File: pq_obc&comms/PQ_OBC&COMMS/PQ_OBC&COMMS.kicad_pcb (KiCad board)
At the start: 4 copper layers, 40 x 40 mm, 66 parts, among them J1 Conn_01x10, J2 Conn_01x10, J3 Conn_01x10, J4 Conn_01x10, J6 U.FL-R-SMT-1_10_, U1 STM32L162RETx, U2 SX1262IMLTRT, U3 BD2232G-GTR, U4 BD2232G-GTR, U5 RFswitch, U7 BD2232G-GTR, X1 12MHz, X2 FA-128_32.0000MF20X-K5, X3 32.768KHz

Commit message: change organization
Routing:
- net GND: vias 36 -> 60
- net (no net): vias 26 -> 2
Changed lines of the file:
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@@
     (effects (font (size 1.5 1.5) (thickness 0.152)) (justify left))
   )
-  (via (at 109.4 69.637) (size 0.4) (drill 0.2) (layers "F.Cu" "B.Cu") (net 0))
-  (via (at 109.59 67.767) (size 0.4) (drill 0.2) (layers "F.Cu" "B.Cu") (net 0))
-  (via (at 97.17 59.687) (size 0.4) (drill 0.2) (layers "F.Cu" "B.Cu") (net 0))
-  (via (at 111.36 66.567) (size 0.4) (drill 0.2) (layers "F.Cu" "B.Cu") (net 0))
-  (via (at 100.43 75.267) (size 0.4) (drill 0.2) (layers "F.Cu" "B.Cu") (net 0))
-  (via (at 99.84 69.147) (size 0.4) (drill 0.2) (layers "F.Cu" "B.Cu") (net 0))
-  (via (at 104.42 71.797) (size 0.4) (drill 0.2) (layers "F.Cu" "B.Cu") (net 0))
-  (via (at 110.89 63.487) (size 0.4) (drill 0.2) (layers "F.Cu" "B.Cu") (net 0))
-  (via (at 100.37 70.387) (size 0.4) (drill 0.2) (layers "F.Cu" "B.Cu") (net 0))
   (via (at 93.31 61.357) (size 0.4) (drill 0.2) (layers "F.Cu" "B.Cu") (net 0))
-  (via (at 109.43 59.107) (size 0.4) (drill 0.2) (layers "F.Cu" "B.Cu") (net 0))
-  (via (at 110.19 65.557) (size 0.4) (drill 0.2) (layers "F.Cu" "B.Cu") (net 0))
-  (via (at 109.57 66.507) (size 0.4) (drill 0.2) (layers "F.Cu" "B.Cu") (net 0))
-  (via (at 110.997 60.004) (size 0.4) (drill 0.2) (layers "F.Cu" "B.Cu") (net 0))
-  (via (at 111.93 58.987) (size 0.4) (drill 0.2) (layers "F.Cu" "B.Cu") (net 0))
-  (via (at 101.7 63.087) (size 0.4) (drill 0.2) (layers "F.Cu" "B.Cu") (net 0))
-  (via (at 111 61.497) (size 0.4) (drill 0.2) (layers "F.Cu" "B.Cu") (net 0))
-  (via (at 111.91 63.987) (size 0.4) (drill 0.2) (layers "F.Cu" "B.Cu") (net 0))
   (via (at 90.81 59.057) (size 0.4) (drill 0.2) (layers "F.Cu" "B.Cu") (net 0))
-  (via (at 97.15 61.097) (size 0.4) (drill 0.2) (layers "F.Cu" "B.Cu") (net 0))
-  (via (at 113.26 57.047) (size 0.4) (drill 0.2) (layers "F.Cu" "B.Cu") (net 0))
-  (via (at 104.12 70.867) (size 0.4) (drill 0.2) (layers "F.Cu" "B.Cu") (net 0))
-  (via (at 110.03 71.827) (size 0.4) (drill 0.2) (layers "F.Cu" "B.Cu") (net 0))
-  (via (at 98.58 71.057) (size 0.4) (drill 0.2) (layers "F.Cu" "B.Cu") (net 0))
-  (via (at 99.29 72.367) (size 0.4) (drill 0.2) (layers "F.Cu" "B.Cu") (net 0))
-  (via (at 103.17 60.897) (size 0.4) (drill 0.2) (layers "F.Cu" "B.Cu") (net 0))
   (segment (start 110.1 58.157) (end 110.1 62.587) (width 0.35) (layer "F.Cu") (net 1))
   (segment (start 109.943 58) (end 110.1 58.157) (width 0.3) (layer "F.Cu") (net 1))
@@
   (segment (start 106.88 70.296) (end 106.88 69.867) (width 0.2) (layer "F.Cu") (net 2))
   (via (at 106.38 75.217) (size 0.4) (drill 0.2) (layers "F.Cu" "B.Cu") (free) (net 2))
+  (via (at 109.4 69.637) (size 0.4) (drill 0.2) (layers "F.Cu" "B.Cu") (free) (net 2))
   (via (at 102.715 69.867) (size 0.4) (drill 0.2) (layers "F.Cu" "B.Cu") (net 2))
+  (via (at 109.59 67.767) (size 0.4) (drill 0.2) (layers "F.Cu" "B.Cu") (free) (net 2))
+  (via (at 97.17 59.687) (size 0.4) (drill 0.2) (layers "F.Cu" "B.Cu") (free) (net 2))
   (via (at 105.66 65.807) (size 0.4) (drill 0.2) (layers "F.Cu" "B.Cu") (net 2))
+  (via (at 111.36 66.567) (size 0.4) (drill 0.2) (layers "F.Cu" "B.Cu") (free) (net 2))
   (via (at 107.09 69.307) (size 0.4) (drill 0.2) (layers "F.Cu" "B.Cu") (net 2))
+  (via (at 100.43 75.267) (size 0.4) (drill 0.2) (layers "F.Cu" "B.Cu") (free) (net 2))
   (via (at 99.18 74.727) (size 0.4) (drill 0.2) (layers "F.Cu" "B.Cu") (net 2))
+  (via (at 99.84 69.147) (size 0.4) (drill 0.2) (layers "F.Cu" "B.Cu") (free) (net 2))
   (via (at 107.14 67.557) (size 0.4) (drill 0.2) (layers "F.Cu" "B.Cu") (net 2))
   (via (at 110.3 70.357) (size 0.4) (drill 0.2) (layers "F.Cu" "B.Cu") (net 2))
+  (via (at 104.42 71.797) (size 0.4) (drill 0.2) (layers "F.Cu" "B.Cu") (free) (net 2))
   (via (at 104.23 60.027) (size 0.4) (drill 0.2) (layers "F.Cu" "B.Cu") (net 2))
+  (via (at 110.89 63.487) (size 0.4) (drill 0.2) (layers "F.Cu" "B.Cu") (free) (net 2))
   (via (at 109.4 60.647) (size 0.4) (drill 0.2) (layers "F.Cu" "B.Cu") (net 2))
+  (via (at 100.37 70.387) (size 0.4) (drill 0.2) (layers "F.Cu" "B.Cu") (free) (net 2))
   (via (at 106.56 55.617) (size 0.4) (drill 0.2) (layers "F.Cu" "B.Cu") (net 2))
   (via (at 105.83 69.307) (size 0.4) (drill 0.2) (layers "F.Cu" "B.Cu") (net 2))
@@
   (via (at 99.08 53.257) (size 0.4) (drill 0.2) (layers "F.Cu" "B.Cu") (net 2))
   (via (at 101.81 74.557) (size 0.4) (drill 0.2) (layers "F.Cu" "B.Cu") (free) (net 2))
+  (via (at 109.43 59.107) (size 0.4) (drill 0.2) (layers "F.Cu" "B.Cu") (free) (net 2))
+  (via (at 110.19 65.557) (size 0.4) (drill 0.2) (layers "F.Cu" "B.Cu") (free) (net 2))
   (via (at 104.79 62.227) (size 0.4) (drill 0.2) (layers "F.Cu" "B.Cu") (free) (net 2))
   (via (at 98.64 69.687) (size 0.4) (drill 0.2) (layers "F.Cu" "B.Cu") (net 2))
+  (via (at 109.57 66.507) (size 0.4) (drill 0.2) (layers "F.Cu" "B.Cu") (free) (net 2))
+  (via (at 110.997 60.004) (size 0.4) (drill 0.2) (layers "F.Cu" "B.Cu") (free) (net 2))
   (via (at 107.14 65.307) (size 0.4) (drill 0.2) (layers "F.Cu" "B.Cu") (net 2))
   (via (at 103.61 64.347) (size 0.4) (drill 0.2) (layers "F.Cu" "B.Cu") (free) (net 2))
+  (via (at 111.93 58.987) (size 0.4) (drill 0.2) (layers "F.Cu" "B.Cu") (free) (net 2))
   (via (at 104.05 73.947) (size 0.4) (drill 0.2) (layers "F.Cu" "B.Cu") (free) (net 2))
   (via (at 107.438 56.545) (size 0.4) (drill 0.2) (layers "F.Cu" "B.Cu") (net 2))
   (via (at 102.92 74.027) (size 0.4) (drill 0.2) (layers "F.Cu" "B.Cu") (free) (net 2))
+  (via (at 101.7 63.087) (size 0.4) (drill 0.2) (layers "F.Cu" "B.Cu") (free) (net 2))
   (via (at 105.67 54.797) (size 0.4) (drill 0.2) (layers "F.Cu" "B.Cu") (net 2))
+  (via (at 111 61.497) (size 0.4) (drill 0.2) (layers "F.Cu" "B.Cu") (free) (net 2))
   (via (at 105.66 67.307) (size 0.4) (drill 0.2) (layers "F.Cu" "B.Cu") (net 2))
+  (via (at 111.91 63.987) (size 0.4) (drill 0.2) (layers "F.Cu" "B.Cu") (free) (net 2))
+  (via (at 97.15 61.097) (size 0.4) (drill 0.2) (layers "F.Cu" "B.Cu") (free) (net 2))
   (via (at 104.8 65.257) (size 0.4) (drill 0.2) (layers "F.Cu" "B.Cu") (free) (net 2))
   (via (at 106.509 56.525) (size 0.4) (drill 0.2) (layers "F.Cu" "B.Cu") (net 2))
+  (via (at 113.26 57.047) (size 0.4) (drill 0.2) (layers "F.Cu" "B.Cu") (free) (net 2))
   (via (at 105.73 73.987) (size 0.4) (drill 0.2) (layers "F.Cu" "B.Cu") (free) (net 2))
   (via (at 107.17 74.217) (size 0.4) (drill 0.2) (layers "F.Cu" "B.Cu") (free) (net 2))
   (via (at 104.81 66.667) (size 0.4) (drill 0.2) (layers "F.Cu" "B.Cu") (net 2))
+  (via (at 104.12 70.867) (size 0.4) (drill 0.2) (layers "F.Cu" "B.Cu") (free) (net 2))
   (via (at 103.61 66.027) (size 0.4) (drill 0.2) (layers "F.Cu" "B.Cu") (free) (net 2))
   (via (at 107.14 62.307) (size 0.4) (drill 0.2) (layers "F.Cu" "B.Cu") (net 2))
   (via (at 105.7 64.057) (size 0.4) (drill 0.2) (layers "F.Cu" "B.Cu") (net 2))
   (via (at 105.66 62.807) (size 0.4) (drill 0.2) (layers "F.Cu" "B.Cu") (free) (net 2))
+  (via (at 110.03 71.827) (size 0.4) (drill 0.2) (layers "F.Cu" "B.Cu") (free) (net 2))
   (via (at 106.56 54.817) (size 0.4) (drill 0.2) (layers "F.Cu" "B.Cu") (net 2))
+  (via (at 98.58 71.057) (size 0.4) (drill 0.2) (layers "F.Cu" "B.Cu") (free) (net 2))
+  (via (at 99.29 72.367) (size 0.4) (drill 0.2) (layers "F.Cu" "B.Cu") (free) (net 2))
   (via (at 104.95 63.127) (size 0.4) (drill 0.2) (layers "F.Cu" "B.Cu") (free) (net 2))
   (via (at 102.42 64.877) (size 0.4) (drill 0.2) (layers "F.Cu" "B.Cu") (free) (net 2))
+  (via (at 103.17 60.897) (size 0.4) (drill 0.2) (layers "F.Cu" "B.Cu") (free) (net 2))
   (segment (start 87.49 76.272) (end 87.49 75.898) (width 0.254) (layer "B.Cu") (net 2))
   (segment (start 98.917 75.768) (end 97.562 75.768) (width 0.254) (layer "B.Cu") (net 2))

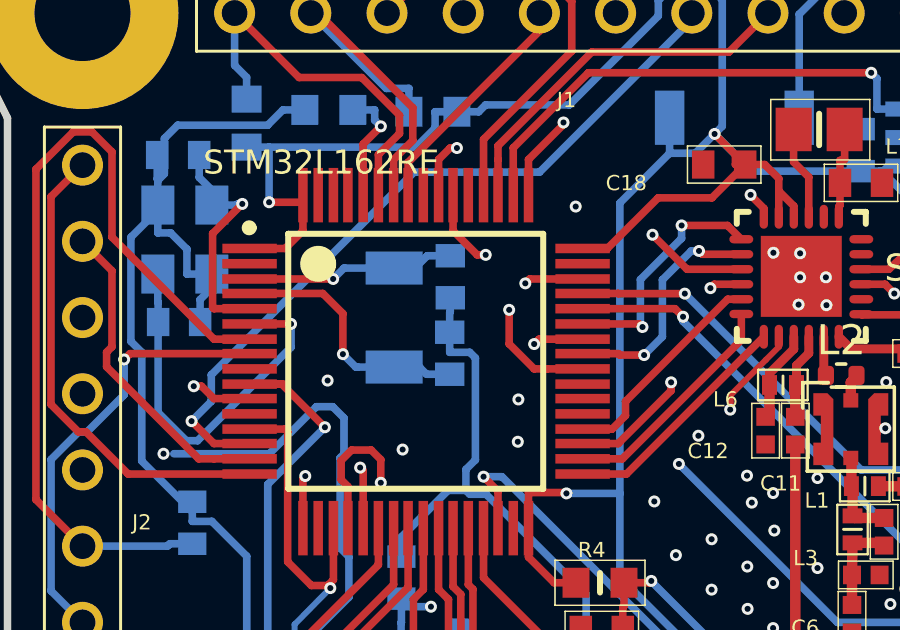
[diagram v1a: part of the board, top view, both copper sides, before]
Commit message: OBC changed to STM32L4, pinout added, EPS ported
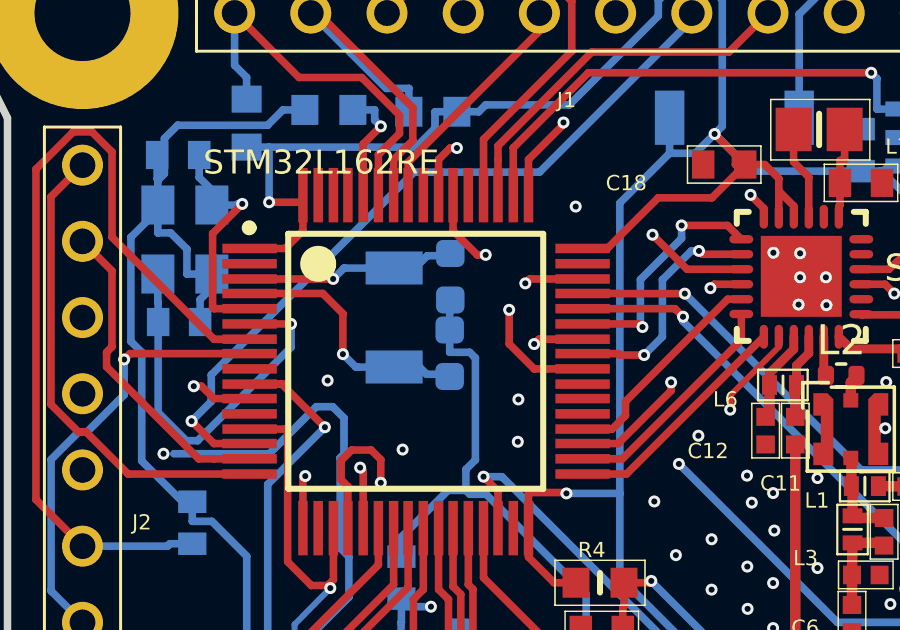
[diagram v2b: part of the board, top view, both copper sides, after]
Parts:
- C38, C39: footprint easyeda:CAPC1608X80N -> Capacitor_SMD:C_0603_1608Metric; moved to B.Cu
- turned C38 to -90 degrees
- turned C39 to 90 degrees
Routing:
- net P/L2BURN_OBC: track 16.5 -> 20.0 mm
- net P/L2BURN: track 3.45 -> 0.00 mm
